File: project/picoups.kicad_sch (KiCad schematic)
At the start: 16 parts, among them J1 Conn_02x20_Odd_Even, J2 BATT, J3 VIN, J5 USB_C_Receptacle, Q1 Q_PMOS_GSD, SW2 SW_SPST, U4 M41T62

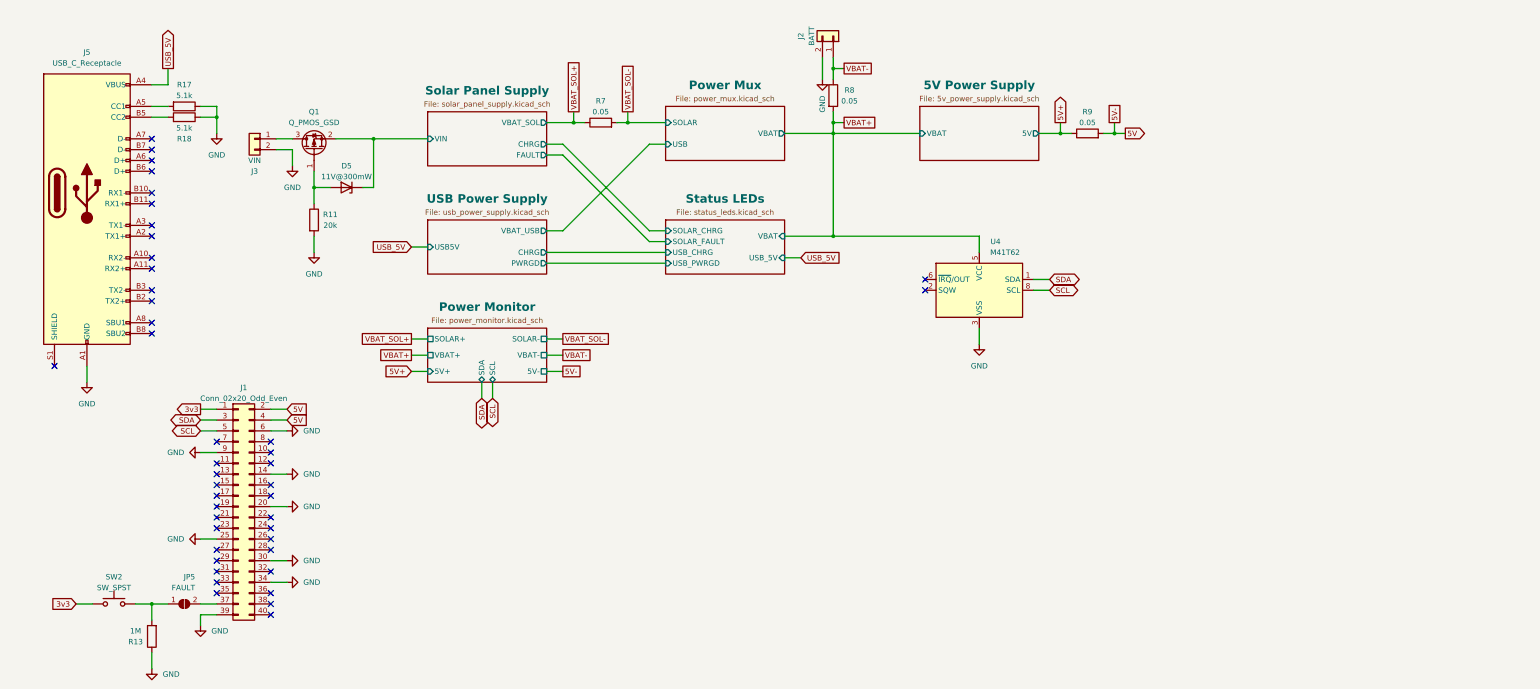
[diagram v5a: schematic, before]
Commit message: Added symbol annotations
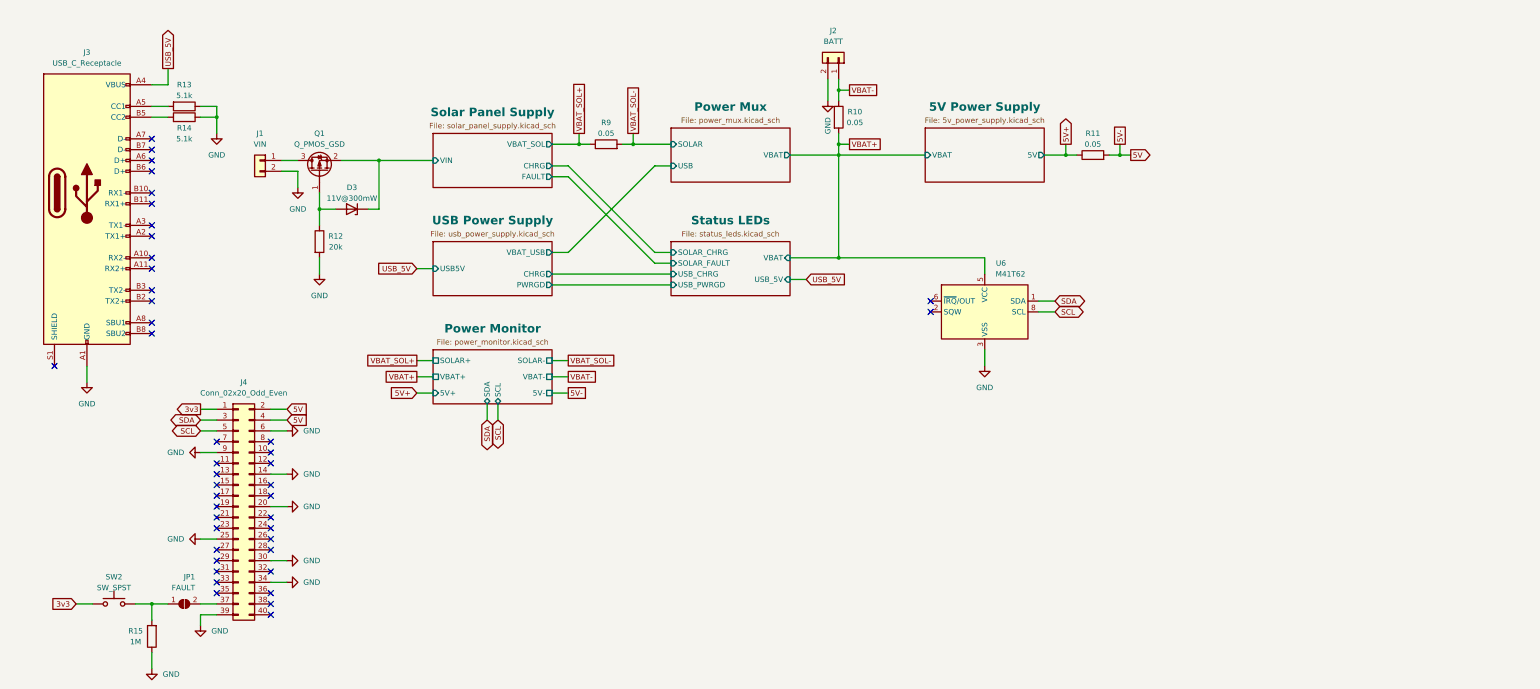
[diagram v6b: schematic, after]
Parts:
- renumbered D5 to D3, J3 to J1, J5 to J3, J1 to J4, JP5 to JP1, R8 to R10, R9 to R11, R11 to R12, R17 to R13, R18 to R14, R13 to R15, R7 to R9, U4 to U6
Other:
- moved on the sheet: D3, J1, J2, Q1, R10, R11, R12, R9, U6

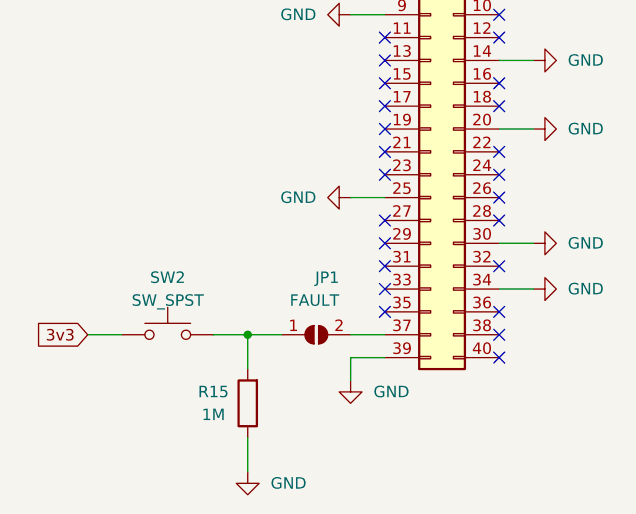
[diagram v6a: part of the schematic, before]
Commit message: Added footprints
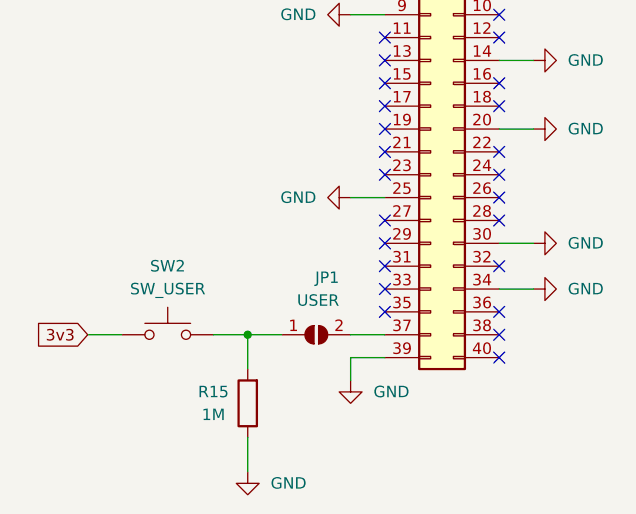
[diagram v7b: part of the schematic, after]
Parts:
- J3: footprint (none) -> Connector_USB:USB_C_Receptacle_G-Switch_GT-USB-7010ASV
- JP1: value FAULT -> USER
- R13, R14: footprint Resistor_SMD:R_0805_2012Metric -> Resistor_SMD:R_0603_1608Metric
- R15: footprint Resistor_SMD:R_1210_3225Metric -> Resistor_SMD:R_0805_2012Metric
- SW2: value SW_SPST -> SW_USER; footprint (none) -> PicoUPS:SW_Push
- U6: footprint (none) -> PicoUPS:LCC-8
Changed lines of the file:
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@@
       (effects (font (size 1.27 1.27)))
     )
-    (property "Footprint" "Resistor_SMD:R_0805_2012Metric" (at 53.34 39.878 90)
+    (property "Footprint" "Resistor_SMD:R_0603_1608Metric" (at 53.34 39.878 90)
       (effects (font (size 1.27 1.27)) hide)
     )
@@
       (effects (font (size 1.27 1.27)))
     )
-    (property "Footprint" "" (at 34.29 55.88 0)
+    (property "Footprint" "Connector_USB:USB_C_Receptacle_G-Switch_GT-USB-7010ASV" (at 34.29 55.88 0)
       (effects (font (size 1.27 1.27)) hide)
     )
@@
       (effects (font (size 1.27 1.27)) (justify left))
     )
-    (property "Footprint" "" (at 241.3 83.82 0)
+    (property "Footprint" "PicoUPS:LCC-8" (at 241.3 83.82 0)
       (effects (font (size 1.27 1.27)) hide)
     )
@@
       (effects (font (size 1.27 1.27)) (justify right))
     )
-    (property "Value" "FAULT" (at 55.88 148.59 0)
+    (property "Value" "USER" (at 55.88 148.59 0)
       (effects (font (size 1.27 1.27)) (justify right))
     )
@@
       (effects (font (size 1.27 1.27)))
     )
-    (property "Footprint" "Resistor_SMD:R_0805_2012Metric" (at 53.34 33.782 90)
+    (property "Footprint" "Resistor_SMD:R_0603_1608Metric" (at 53.34 33.782 90)
       (effects (font (size 1.27 1.27)) hide)
     )
@@
   (symbol (lib_id "Switch:SW_Push") (at 36.83 152.4 0) (unit 1)
     (in_bom yes) (on_board yes) (dnp no) (fields_autoplaced)
-    (property "Reference" "SW2" (at 36.83 146.05 0)
-      (effects (font (size 1.27 1.27)))
-    )
-    (property "Value" "SW_SPST" (at 36.83 148.59 0)
-      (effects (font (size 1.27 1.27)))
-    )
-    (property "Footprint" "" (at 36.83 147.32 0)
+    (property "Reference" "SW2" (at 36.83 144.78 0)
+      (effects (font (size 1.27 1.27)))
+    )
+    (property "Value" "SW_USER" (at 36.83 147.32 0)
+      (effects (font (size 1.27 1.27)))
+    )
+    (property "Footprint" "PicoUPS:SW_Push" (at 36.83 147.32 0)
       (effects (font (size 1.27 1.27)) hide)
     )
@@
       (effects (font (size 1.27 1.27)))
     )
-    (property "Footprint" "Resistor_SMD:R_1210_3225Metric" (at 47.498 160.02 90)
-      (effects (font (size 1.27 1.27)) hide)
-    )
+    (property "Footprint" "Resistor_SMD:R_0805_2012Metric" (at 47.498 160.02 90)
+      (effects (font (size 1.27 1.27)) hide)
+    )

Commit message: Basic layout
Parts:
- J3: footprint Connector_USB:USB_C_Receptacle_G-Switch_GT-USB-7010ASV -> Connector_USB:USB_C_Receptacle_GCT_USB4105-xx-A_16P_TopMnt_Horizontal
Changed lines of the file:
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@@
       (effects (font (size 1.27 1.27)))
     )
-    (property "Footprint" "Connector_USB:USB_C_Receptacle_G-Switch_GT-USB-7010ASV" (at 34.29 55.88 0)
+    (property "Footprint" "Connector_USB:USB_C_Receptacle_GCT_USB4105-xx-A_16P_TopMnt_Horizontal" (at 34.29 55.88 0)
       (effects (font (size 1.27 1.27)) hide)
     )
